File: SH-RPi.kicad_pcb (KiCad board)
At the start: 4 copper layers, 86 x 56 mm, 149 parts, among them J501 JST XH horiz, J502 Wire Link, J601 Conn_02x07_Counter_Clockwise, J602 Conn_01x02, J702 Raspberry_Pi_2_3, J801 JST XH horiz, J802 Wire Link, Q501 PJA3441, SW201 SW_SPST, U201 TPS61022, U301 H7533-H#, U302 LMR14050SDDA, U303 MD1322, U401 DS3231MZ, U601 ATtiny1614-SSNR, U602 RCLAMP0524P-N, U802 H7550-H#, U803 MCP2515-xST, U804 ISO1050DUB, Y801 X322516MLB4SI

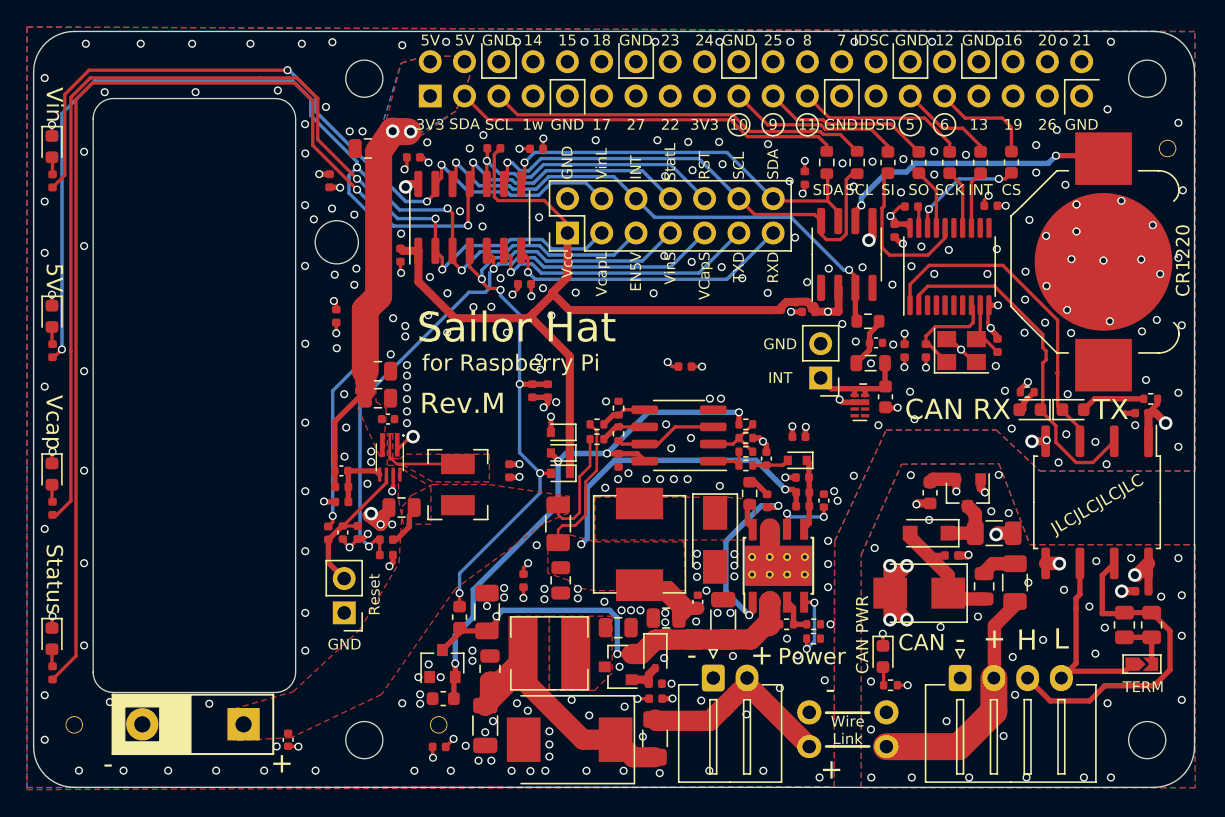
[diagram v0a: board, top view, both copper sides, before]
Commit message: Add HL logo, change versioning scheme
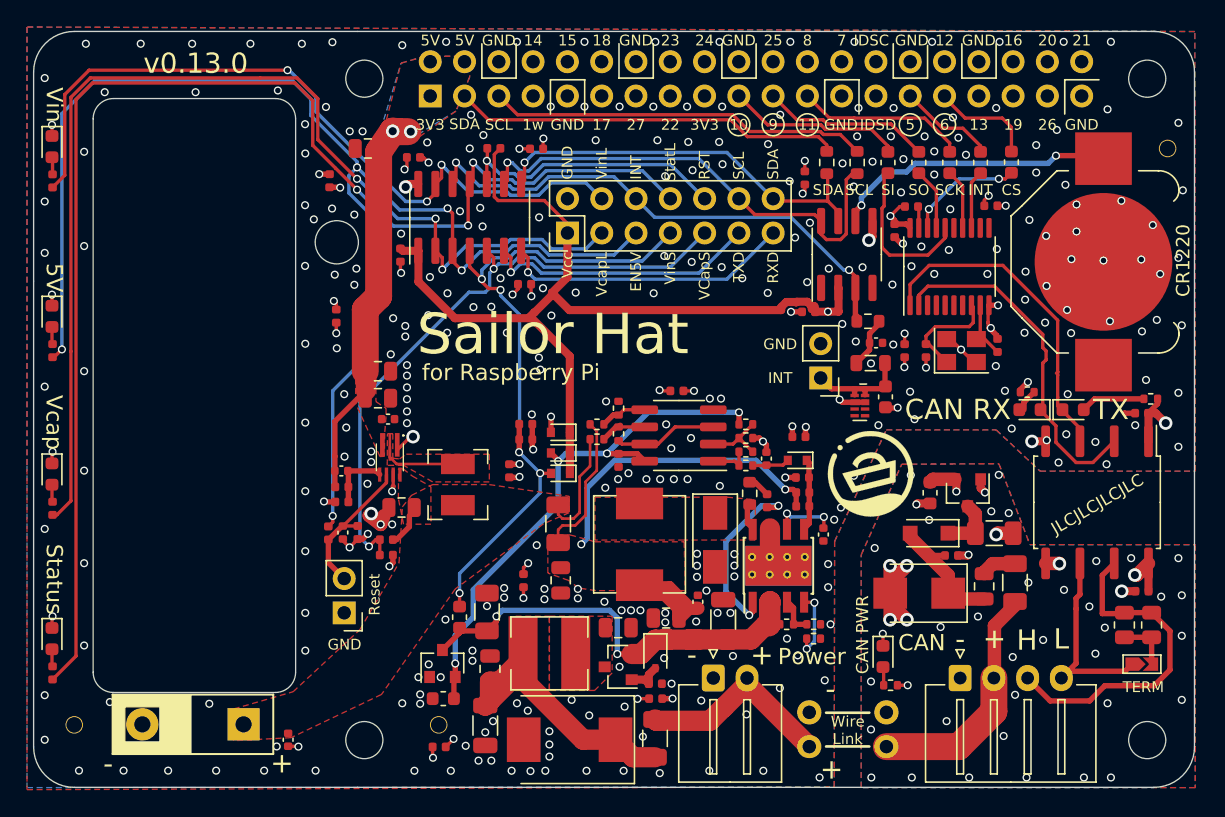
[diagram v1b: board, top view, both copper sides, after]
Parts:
- added G***: LOGO, SH-RPi:HL_pictogram_6.3mm, F.Cu at (81.0, 63.1)
- moved C601 3.64 mm to (55.4, 60.6), turned to 0 degrees
- moved R602 2.96 mm to (55.4, 59.4), turned to 0 degrees
- moved C308 2.51 mm to (77.5, 67.6), turned to 270 degrees
- moved C914 1.90 mm to (66.6, 57.0)
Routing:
- net GND: track 49.1 -> 49.0 mm, vias 314 -> 332
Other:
- board text added: "v0.13.0"
- board text removed: "Rev.M"

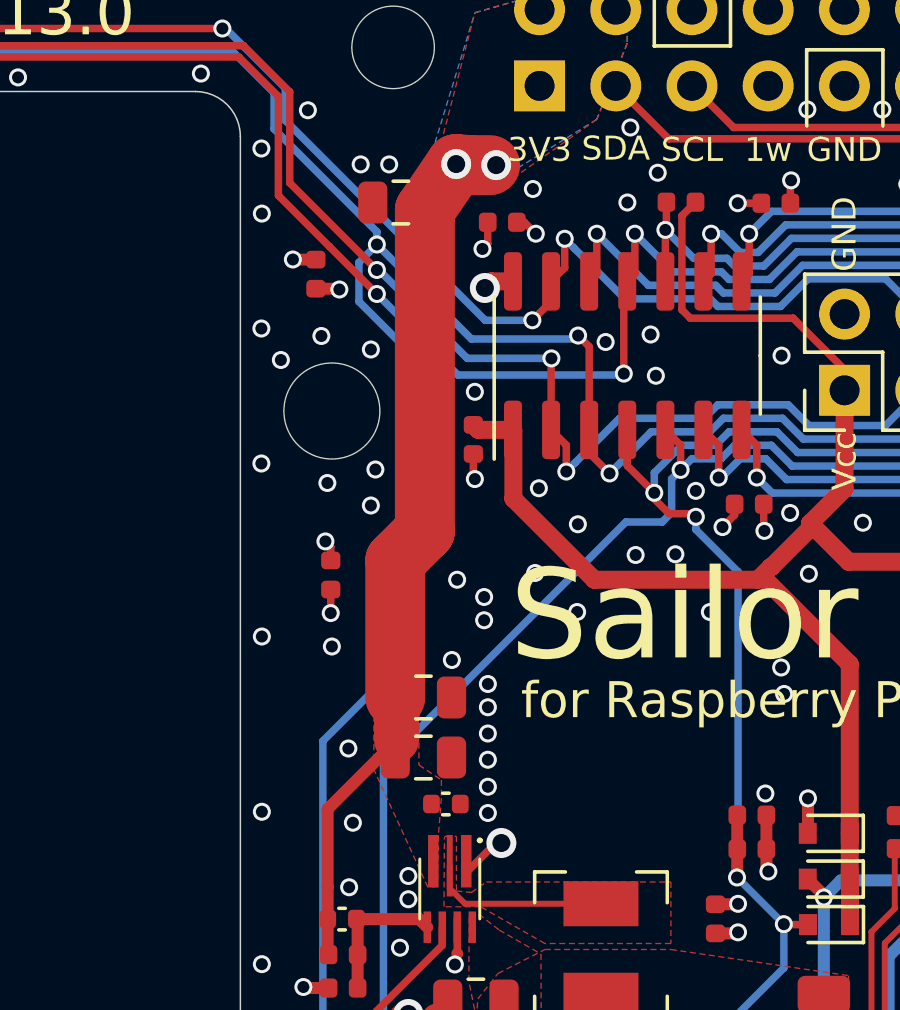
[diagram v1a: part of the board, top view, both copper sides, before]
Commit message: Add a 5V header for fans etc
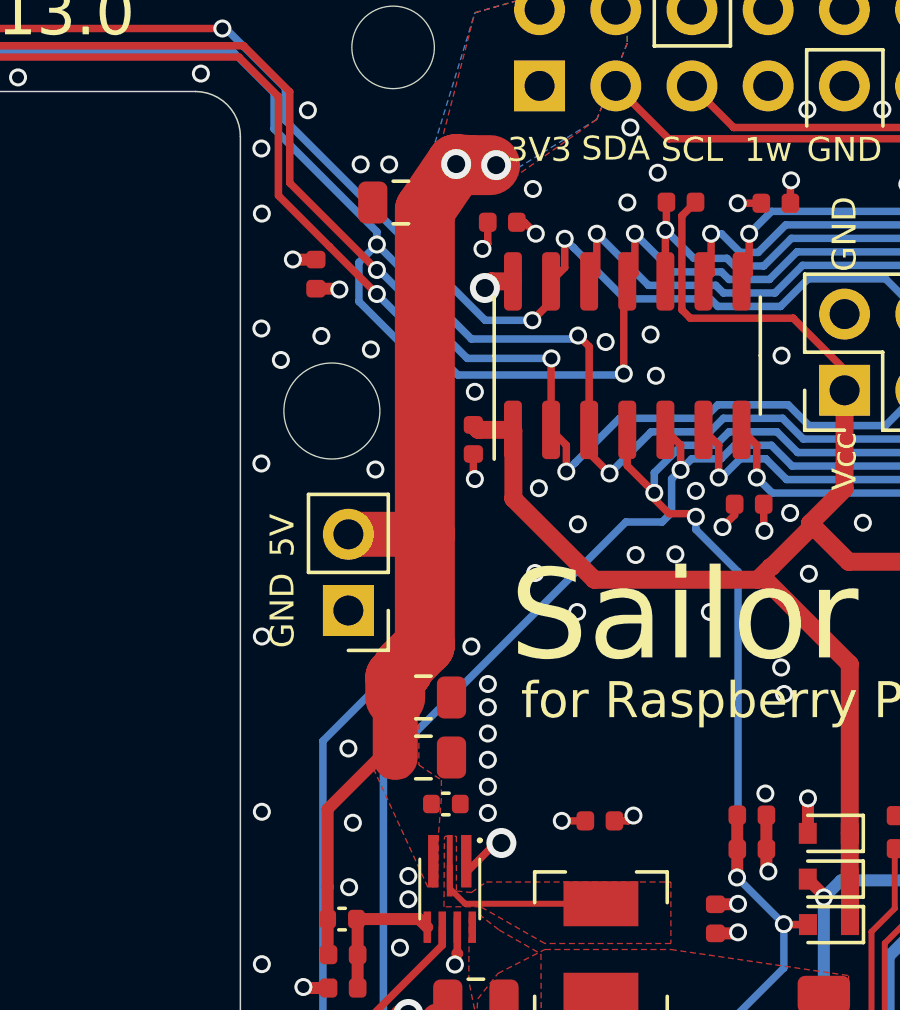
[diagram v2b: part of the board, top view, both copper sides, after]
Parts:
- added J701: Conn_01x02, Connector_PinHeader_2.54mm:PinHeader_1x02_P2.54mm_Vertical, F.Cu at (42.0, 52.6)
- moved C901 12.2 mm to (50.4, 59.6), turned to 180 degrees
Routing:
- net GND: vias 332 -> 326

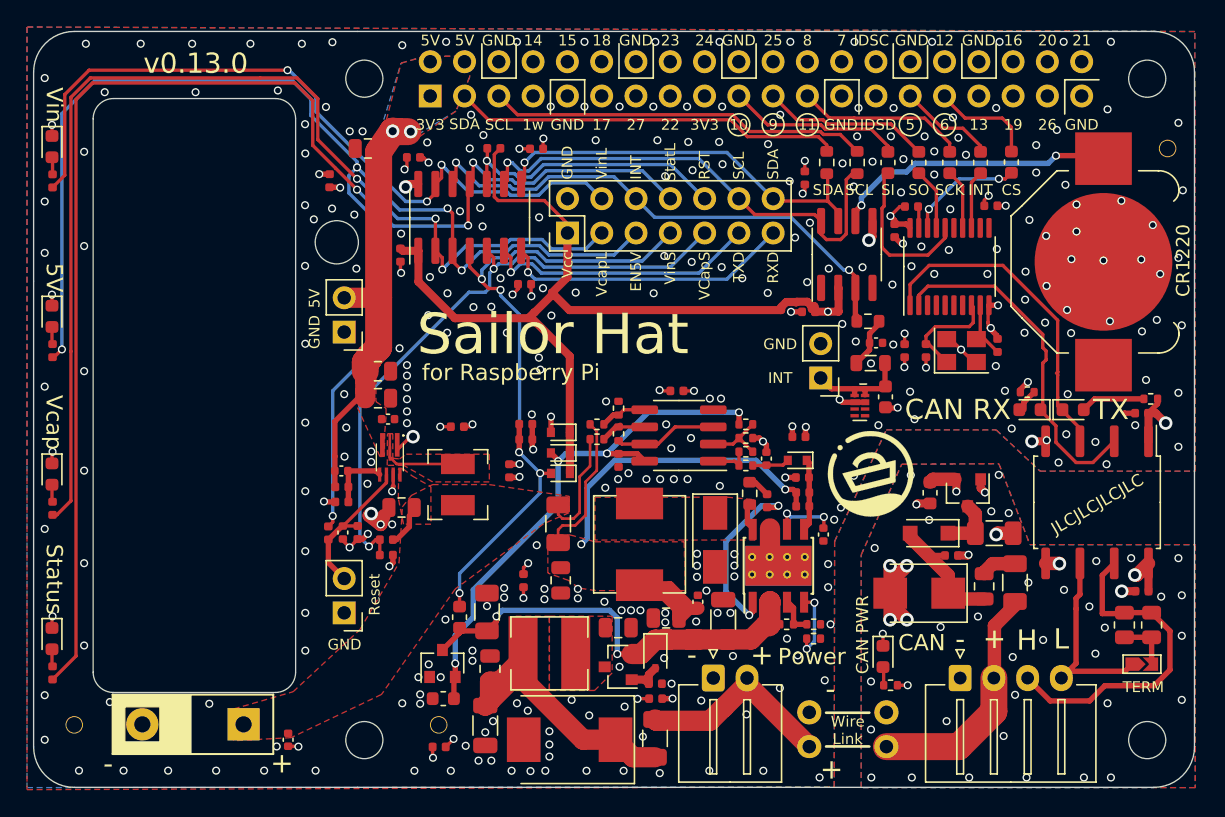
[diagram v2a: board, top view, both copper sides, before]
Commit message: Tweak components according to JLCPCB availability
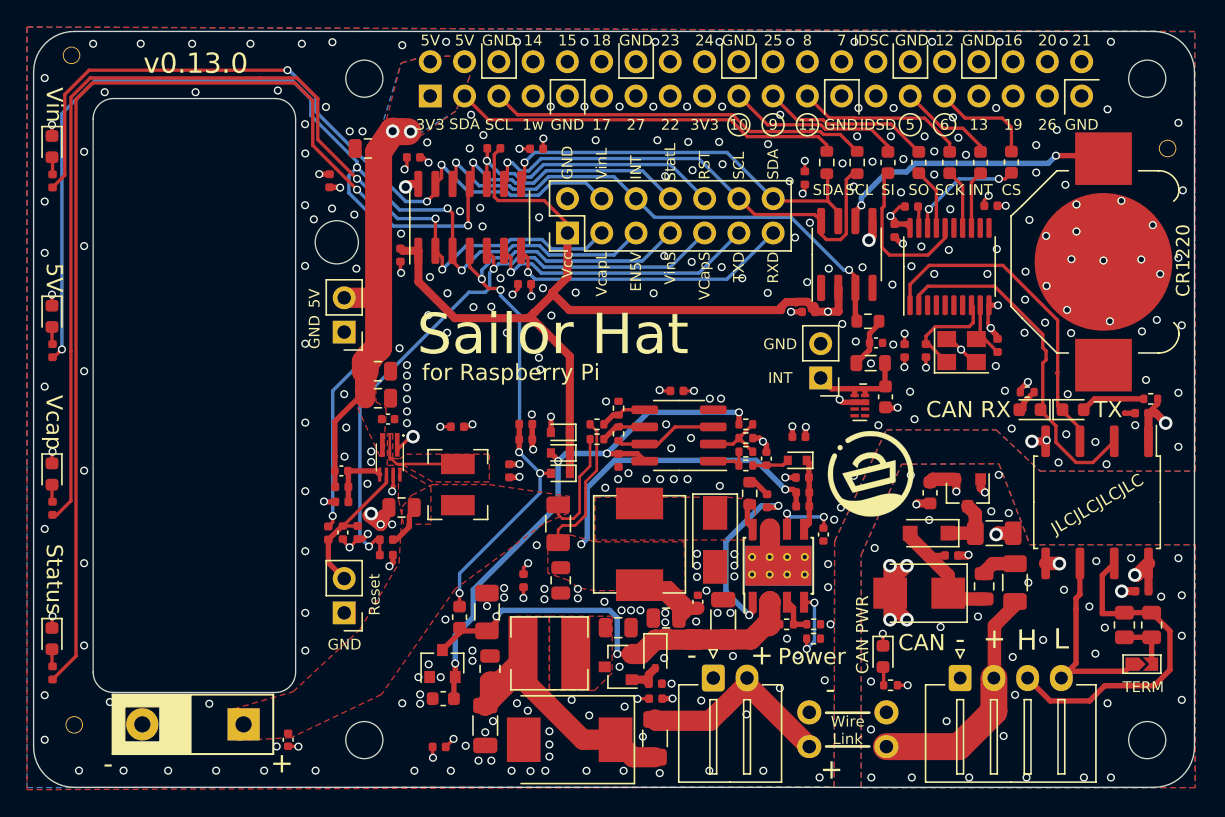
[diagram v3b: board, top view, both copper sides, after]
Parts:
- L301: value MWSA0603S-3R3MT -> MHCI06040-3R3M-R8
- Q501: value PJA3441 -> 5P40
- moved H902 56.6 mm to (21.8, 32.1)
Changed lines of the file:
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@@
     (descr "Through hole straight pin header, 1x02, 2.54mm pitch, single row")
     (tags "Through hole pin header THT 1x02 2.54mm single row")
+    (attr virtual)
     (fp_text reference J701 (at 0 -2.33) (layer F.SilkS) hide
       (effects (font (size 1 1) (thickness 0.15)))
@@
     (descr "Through hole straight pin header, 2x20, 2.54mm pitch, double rows")
     (tags "Through hole pin header THT 2x20 2.54mm double row")
+    (attr virtual)
     (fp_text reference J702 (at 1.27 -2.33 90) (layer F.SilkS) hide
       (effects (font (size 1 1) (thickness 0.15)))
@@
       (effects (font (size 1 1) (thickness 0.15)))
     )
-    (fp_text value MWSA0603S-3R3MT (at 0 4.1 90) (layer F.Fab) hide
+    (fp_text value MHCI06040-3R3M-R8 (at 0 4.1 90) (layer F.Fab) hide
       (effects (font (size 1 1) (thickness 0.15)))
     )
@@
   )
   (module SH-RPi:JlcpcbToolingHole (layer F.Cu)
-    (at 49 81.7)
+    (at 21.8 32.1)
     (fp_text reference H902 (at 0 2.1) (layer F.SilkS) hide
       (effects (font (size 1 1) (thickness 0.15)))
@@
     (descr "JST XH series connector, S4B-XH-A-1 (http://www.jst-mfg.com/product/pdf/eng/eXH.pdf), generated with kicad-footprint-generator")
     (tags "connector JST XH horizontal")
+    (attr virtual)
     (fp_text reference J801 (at 3.8 -1.7) (layer F.SilkS) hide
       (effects (font (size 1 1) (thickness 0.15)))
@@
     (descr "JST XH series connector, S2B-XH-A-1 (http://www.jst-mfg.com/product/pdf/eng/eXH.pdf), generated with kicad-footprint-generator")
     (tags "connector JST XH horizontal")
+    (attr virtual)
     (fp_text reference J501 (at 3 -1.8) (layer F.SilkS) hide
       (effects (font (size 1 1) (thickness 0.15)))
@@
     (descr "Through hole straight pin header, 2x07, 2.54mm pitch, double rows")
     (tags "Through hole pin header THT 2x07 2.54mm double row")
+    (attr virtual)
     (fp_text reference J601 (at 1.27 -2.33 90) (layer F.SilkS) hide
       (effects (font (size 1 1) (thickness 0.15)))
@@
       (effects (font (size 1 1) (thickness 0.15)))
     )
-    (fp_text value PJA3441 (at 0 2.5) (layer F.Fab) hide
+    (fp_text value 5P40 (at 0 2.5) (layer F.Fab) hide
       (effects (font (size 1 1) (thickness 0.15)))
     )
@@
   (gr_arc (start 36.9 36.8) (end 38.4 36.8) (angle -90) (layer Edge.Cuts) (width 0.05))
   (gr_arc (start 24.9 36.8) (end 24.9 35.3) (angle -90) (layer Edge.Cuts) (width 0.05))
-  (gr_text TX (at 98.8 58.35) (layer F.SilkS)
-    (effects (font (size 1.5 1.5) (thickness 0.3)))
+  (gr_text TX (at 98.6 58.35) (layer F.SilkS)
+    (effects (font (size 1.2 1.2) (thickness 0.25)))
   )
   (gr_text "CAN RX" (at 91.4 58.35) (layer F.SilkS)
-    (effects (font (size 1.5 1.5) (thickness 0.3)) (justify right))
+    (effects (font (size 1.2 1.2) (thickness 0.25)) (justify right))
   )
   (gr_line (start 21.9 77.25) (end 21.9 37.3) (layer Cmts.User) (width 0.1))
@@
   (via (at 19.812 79.502) (size 0.6) (drill 0.4) (layers F.Cu B.Cu) (net 1))
   (via (at 19.812 33.782) (size 0.6) (drill 0.4) (layers F.Cu B.Cu) (net 1))
-  (via (at 22.86 31.242) (size 0.6) (drill 0.4) (layers F.Cu B.Cu) (net 1))
+  (via (at 23.4 31.242) (size 0.6) (drill 0.4) (layers F.Cu B.Cu) (net 1))
   (via (at 26.924 31.242) (size 0.6) (drill 0.4) (layers F.Cu B.Cu) (net 1))
   (via (at 30.734 31.242) (size 0.6) (drill 0.4) (layers F.Cu B.Cu) (net 1))

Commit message: Bump version number to 1.0.0
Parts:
- moved C901 0.90 mm to (50.4, 58.7)
- moved C907 0.59 mm to (54.8, 62.9), turned to 0 degrees
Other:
- board text added: "v1.0.0"
- board text removed: "v0.13.0"

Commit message: Add the WEEE logo
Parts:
- added REF**: WEEE-Logo_4.2x6mm_SilkScreen, Symbol:WEEE-Logo_4.2x6mm_SilkScreen, B.Cu at (78.3, 75.5)
- moved REF** 4.05 mm to (60.3, 79.3)

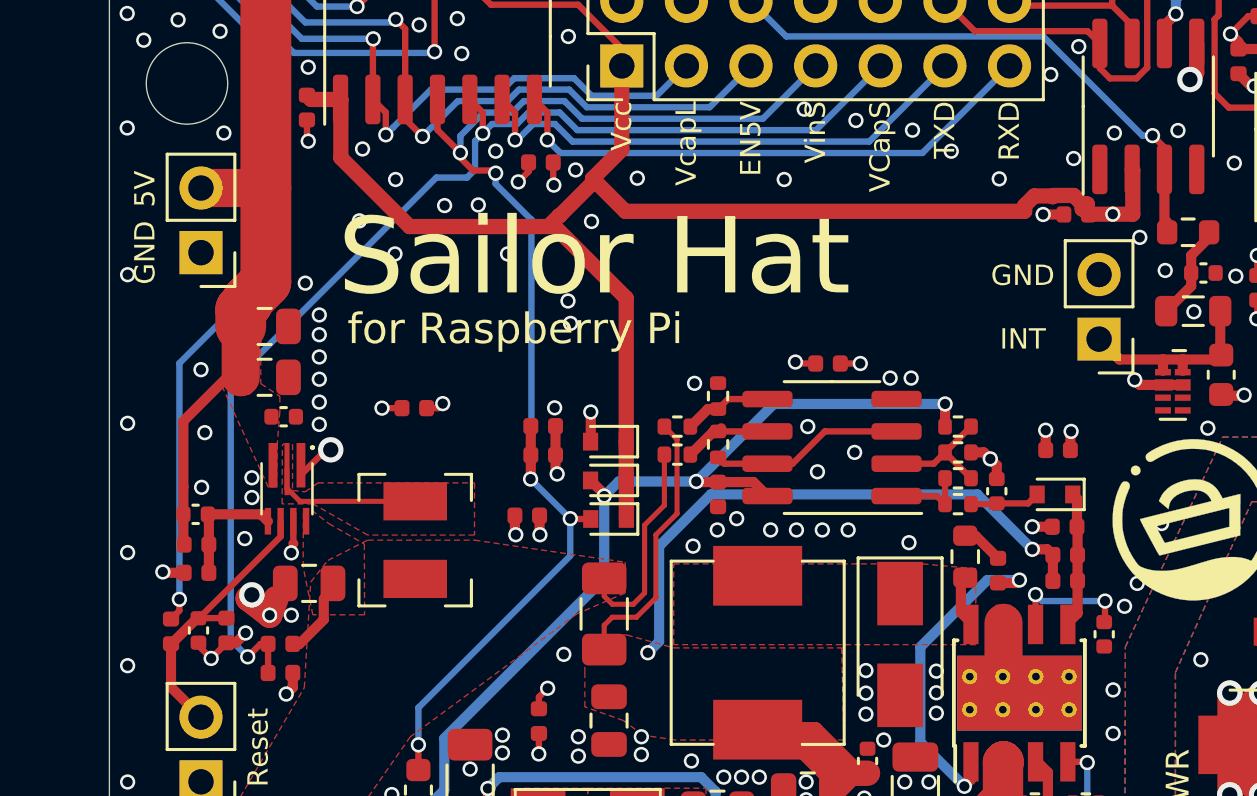
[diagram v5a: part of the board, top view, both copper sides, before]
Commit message: Tweak boost config according to TI SLVAES4
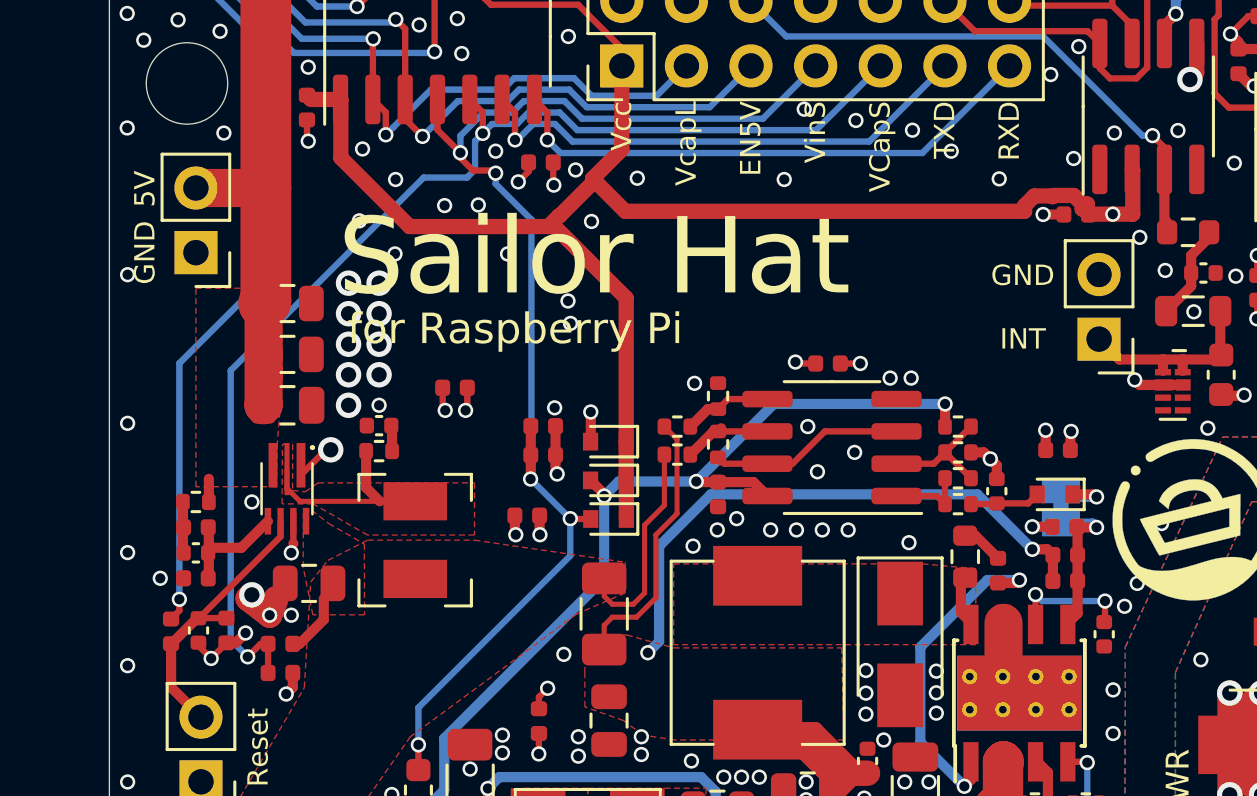
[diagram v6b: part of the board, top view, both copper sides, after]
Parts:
- added C208: 100pF, Capacitor_SMD:C_0402_1005Metric, F.Cu at (49.0, 59.4)
- added JP301: Bridged, Jumper:SolderJumper-2_P1.3mm_Bridged_Pad1.0x1.5mm, B.Cu at (75.8, 62.6)
- added R205: 49.9, Resistor_SMD:R_0402_1005Metric, F.Cu at (41.8, 62.4)
- added R206: 10.0R, Resistor_SMD:R_0402_1005Metric, F.Cu at (49.0, 60.4)
- C205: value 1pF -> 100pF
- C207: value 1uF/25V -> 22uF/25V; footprint Capacitor_SMD:C_0402_1005Metric -> Capacitor_SMD:C_0805_2012Metric
- R203: value 150k -> 750k
- R204: value 20k -> 100k
- moved C901 1.79 mm to (52.0, 57.9)
- moved C205 1.51 mm to (41.8, 64.4)
- moved C202 1.27 mm to (45.4, 56.6)
- moved C204 1.27 mm to (45.4, 54.6)
- moved R203 0.67 mm to (41.8, 63.4)
- moved C207 0.47 mm to (45.4, 58.6)
- moved R204 0.22 mm to (41.8, 65.4)
- moved J701 0.20 mm to (41.8, 52.6)
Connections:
- C205 pad 2: 5V -> Net-(C205-Pad2)
- D302 pad 1: /Buck converter/FB -> Net-(D302-Pad1)
- R203 pad 1: 5V -> Net-(C205-Pad2)
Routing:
- net 5V: track 32.3 -> 26.4 mm
- net Net-(D302-Pad1): track 0.00 -> 2.48 mm, vias 0 -> 1
- net /Boost converter/SW: track 6.24 -> 8.44 mm
- net Net-(C205-Pad2): track 0.00 -> 1.97 mm
- net Net-(C208-Pad2): track 0.00 -> 1.01 mm
- net /Buck converter/FB: track 5.31 -> 6.22 mm, vias 0 -> 1
- net GND: track 49.0 -> 48.3 mm, vias 326 -> 324
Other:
- board text added: "Dis. Cur Lim"

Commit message: Bump version, update license
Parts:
- removed the G*** at (47.8, 42.2)
- added G***: LOGO, SH-RPi:cc-by_5mm, B.Cu at (44.0, 41.6)
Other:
- board text added: "v1.0.1"
- board text removed: "v1.0.0"
